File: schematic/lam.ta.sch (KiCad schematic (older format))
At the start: 14 parts, among them J1 Arduino_Nano_Header, P1 CONN_LED0, P10 CONN_TOUCH3, P2 CONN_LED1, P3 CONN_LED2, P4 CONN_LED3, P5 CONN_PSU, P6 CONN_LINE_IN, P7 CONN_TOUCH0, P8 CONN_TOUCH1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

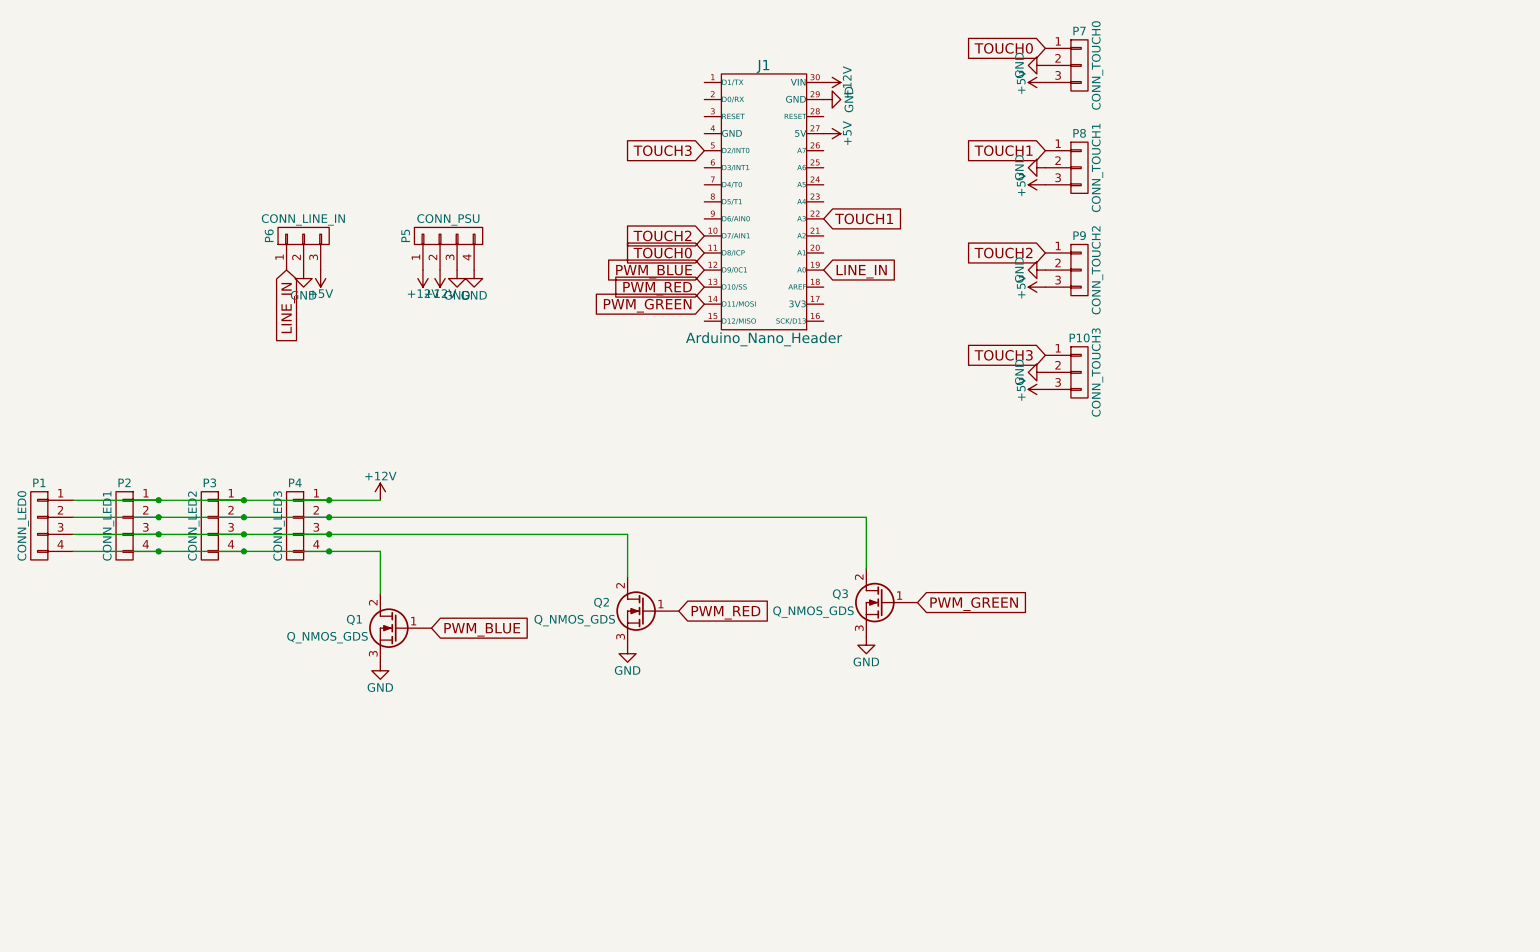
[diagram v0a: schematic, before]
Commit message: Update schematic license, replace AT42QT101X with MPR121
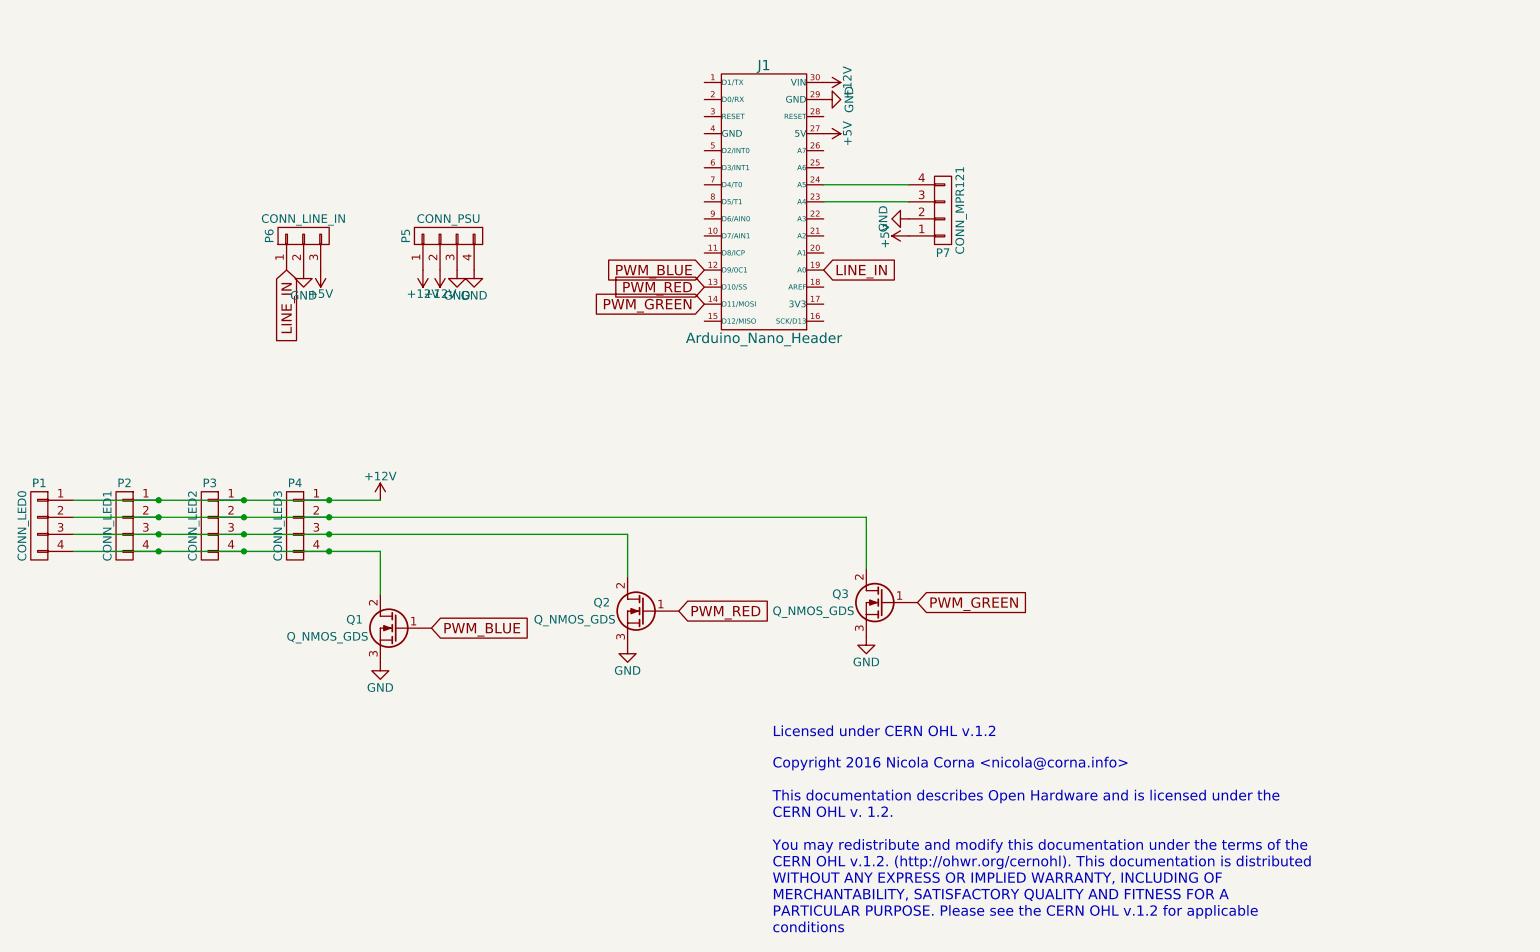
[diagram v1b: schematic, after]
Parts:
- removed P10: CONN_TOUCH3, Pin_Headers:Pin_Header_Straight_1x03, symbol CONN_01X03
- removed P7: CONN_TOUCH0, Pin_Headers:Pin_Header_Straight_1x03, symbol CONN_01X03
- removed P8: CONN_TOUCH1, Pin_Headers:Pin_Header_Straight_1x03, symbol CONN_01X03
- removed P9: CONN_TOUCH2, Pin_Headers:Pin_Header_Straight_1x03, symbol CONN_01X03
- added P7: CONN_MPR121, Pin_Headers:Pin_Header_Straight_1x04, symbol CONN_01X04
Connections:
- net +5V: now also P7.1 (P1)
- net GND: now also P7.2 (P2)
- net at J1.23 (A4): now also P7.3 (P3)
- net at J1.24 (A5): now also P7.4 (P4)
- net TOUCH0: no longer names the net of J1.11 (D8/ICP)
- net TOUCH1: no longer names the net of J1.22 (A3)
- net TOUCH2: no longer names the net of J1.10 (D7/AIN1)
- net TOUCH3: no longer names the net of J1.5 (D2/INT0)
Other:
- note added: "Copyright 2016 Nicola Corna <nicola@corna.info>\n\nThis documentation describes Open Hardware and is licensed under the\nCERN OHL v. 1.2.\n\nYou may redistribute and modify this documentation under the terms of the\nCERN OHL v.1.2. (http://ohwr.org/cernohl). This documentation is distributed\nWITHOUT ANY EXPRESS OR IMPLIED WARRANTY, INCLUDING OF\nMERCHANTABILITY, SATISFACTORY QUALITY AND FITNESS 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"
- note added: "Licensed under CERN OHL v.1.2"
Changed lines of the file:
@@
 encoding utf-8
 Sheet 1 1
-Title ""
-Date ""
-Rev ""
-Comp ""
-Comment1 ""
+Title "LAM.TA"
+Date "2016-03-14"
+Rev "1.0"
+Comp "Nicola Corna"
+Comment1 "Copyright 2016 Nicola Corna <nicola@corna.info>"
 Comment2 ""
 Comment3 ""
@@
 	1    0    0    -1
 $EndComp
-Text GLabel 6700 2350 0    60   Input ~ 0
-TOUCH0
-Text GLabel 7400 2150 2    60   Input ~ 0
-TOUCH1
-Text GLabel 6700 2250 0    60   Input ~ 0
-TOUCH2
-Text GLabel 6700 1750 0    60   Input ~ 0
-TOUCH3
-$Comp
-L CONN_01X03 P7
-U 1 1 56CADC43
-P 8900 1250
-F 0 "P7" H 8900 1450 50  0000 C CNN
-F 1 "CONN_TOUCH0" V 9000 1250 50  0000 C CNN
-F 2 "Pin_Headers:Pin_Header_Straight_1x03" H 8900 1250 50  0001 C CNN
-F 3 "" H 8900 1250 50  0000 C CNN
-	1    8900 1250
-	1    0    0    -1
-$EndComp
 $Comp
 L GND #PWR01
-U 1 1 56CADCB2
-P 8700 1250
-F 0 "#PWR01" H 8700 1000 50  0001 C CNN
-F 1 "GND" H 8700 1100 50  0000 C CNN
-F 2 "" H 8700 1250 50  0000 C CNN
-F 3 "" H 8700 1250 50  0000 C CNN
-	1    8700 1250
-	0    1    1    0
-$EndComp
-Text GLabel 8700 1150 0    60   Input ~ 0
-TOUCH0
-$Comp
-L CONN_01X03 P8
-U 1 1 56CADD7C
-P 8900 1850
-F 0 "P8" H 8900 2050 50  0000 C CNN
-F 1 "CONN_TOUCH1" V 9000 1850 50  0000 C CNN
-F 2 "Pin_Headers:Pin_Header_Straight_1x03" H 8900 1850 50  0001 C CNN
-F 3 "" H 8900 1850 50  0000 C CNN
-	1    8900 1850
-	1    0    0    -1
-$EndComp
-$Comp
-L GND #PWR02
-U 1 1 56CADD82
-P 8700 1850
-F 0 "#PWR02" H 8700 1600 50  0001 C CNN
-F 1 "GND" H 8700 1700 50  0000 C CNN
-F 2 "" H 8700 1850 50  0000 C CNN
-F 3 "" H 8700 1850 50  0000 C CNN
-	1    8700 1850
-	0    1    1    0
-$EndComp
-Text GLabel 8700 1750 0    60   Input ~ 0
-TOUCH1
-$Comp
-L CONN_01X03 P9
-U 1 1 56CADDB1
-P 8900 2450
-F 0 "P9" H 8900 2650 50  0000 C CNN
-F 1 "CONN_TOUCH2" V 9000 2450 50  0000 C CNN
-F 2 "Pin_Headers:Pin_Header_Straight_1x03" H 8900 2450 50  0001 C CNN
-F 3 "" H 8900 2450 50  0000 C CNN
-	1    8900 2450
-	1    0    0    -1
-$EndComp
-$Comp
-L GND #PWR03
-U 1 1 56CADDB7
-P 8700 2450
-F 0 "#PWR03" H 8700 2200 50  0001 C CNN
-F 1 "GND" H 8700 2300 50  0000 C CNN
-F 2 "" H 8700 2450 50  0000 C CNN
-F 3 "" H 8700 2450 50  0000 C CNN
-	1    8700 2450
-	0    1    1    0
-$EndComp
-Text GLabel 8700 2350 0    60   Input ~ 0
-TOUCH2
-$Comp
-L CONN_01X03 P10
-U 1 1 56CADDF4
-P 8900 3050
-F 0 "P10" H 8900 3250 50  0000 C CNN
-F 1 "CONN_TOUCH3" V 9000 3050 50  0000 C CNN
-F 2 "Pin_Headers:Pin_Header_Straight_1x03" H 8900 3050 50  0001 C CNN
-F 3 "" H 8900 3050 50  0000 C CNN
-	1    8900 3050
-	1    0    0    -1
-$EndComp
-$Comp
-L GND #PWR04
-U 1 1 56CADDFA
-P 8700 3050
-F 0 "#PWR04" H 8700 2800 50  0001 C CNN
-F 1 "GND" H 8700 2900 50  0000 C CNN
-F 2 "" H 8700 3050 50  0000 C CNN
-F 3 "" H 8700 3050 50  0000 C CNN
-	1    8700 3050
-	0    1    1    0
-$EndComp
-Text GLabel 8700 2950 0    60   Input ~ 0
-TOUCH3
-$Comp
-L +5V #PWR05
-U 1 1 56CADEBE
-P 8700 1350
-F 0 "#PWR05" H 8700 1200 50  0001 C CNN
-F 1 "+5V" H 8700 1490 50  0000 C CNN
-F 2 "" H 8700 1350 50  0000 C CNN
-F 3 "" H 8700 1350 50  0000 C CNN
-	1    8700 1350
-	0    -1   -1   0
-$EndComp
-$Comp
-L +5V #PWR06
-U 1 1 56CADED8
-P 8700 1950
-F 0 "#PWR06" H 8700 1800 50  0001 C CNN
-F 1 "+5V" H 8700 2090 50  0000 C CNN
-F 2 "" H 8700 1950 50  0000 C CNN
-F 3 "" H 8700 1950 50  0000 C CNN
-	1    8700 1950
-	0    -1   -1   0
-$EndComp
-$Comp
-L +5V #PWR07
-U 1 1 56CADEF2
-P 8700 2550
-F 0 "#PWR07" H 8700 2400 50  0001 C CNN
-F 1 "+5V" H 8700 2690 50  0000 C CNN
-F 2 "" H 8700 2550 50  0000 C CNN
-F 3 "" H 8700 2550 50  0000 C CNN
-	1    8700 2550
-	0    -1   -1   0
-$EndComp
-$Comp
-L +5V #PWR08
-U 1 1 56CADF0C
-P 8700 3150
-F 0 "#PWR08" H 8700 3000 50  0001 C CNN
-F 1 "+5V" H 8700 3290 50  0000 C CNN
-F 2 "" H 8700 3150 50  0000 C CNN
-F 3 "" H 8700 3150 50  0000 C CNN
-	1    8700 3150
-	0    -1   -1   0
-$EndComp
-$Comp
-L GND #PWR09
 U 1 1 56CAE7F3
 P 7400 1450
-F 0 "#PWR09" H 7400 1200 50  0001 C CNN
+F 0 "#PWR01" H 7400 1200 50  0001 C CNN
 F 1 "GND" H 7400 1300 50  0000 C CNN
 F 2 "" H 7400 1450 50  0000 C CNN
@@
 $EndComp
 $Comp
-L +12V #PWR010
+L +12V #PWR02
 U 1 1 56CB1BE7
 P 4800 3800
-F 0 "#PWR010" H 4800 3650 50  0001 C CNN
+F 0 "#PWR02" H 4800 3650 50  0001 C CNN
 F 1 "+12V" H 4800 3940 50  0000 C CNN
 F 2 "" H 4800 3800 50  0000 C CNN
@@
 $EndComp
 $Comp
-L +12V #PWR011
+L +12V #PWR03
 U 1 1 56CB2CF0
 P 5050 2450
-F 0 "#PWR011" H 5050 2300 50  0001 C CNN
+F 0 "#PWR03" H 5050 2300 50  0001 C CNN
 F 1 "+12V" H 5050 2590 50  0000 C CNN
 F 2 "" H 5050 2450 50  0000 C CNN
@@
 $EndComp
 $Comp
-L +12V #PWR012
+L +12V #PWR04
 U 1 1 56CC30C5
 P 5150 2450
-F 0 "#PWR012" H 5150 2300 50  0001 C CNN
+F 0 "#PWR04" H 5150 2300 50  0001 C CNN
 F 1 "+12V" H 5150 2590 50  0000 C CNN
 F 2 "" H 5150 2450 50  0000 C CNN
@@
 $EndComp
 $Comp
-L GND #PWR013
+L GND #PWR05
 U 1 1 56CF1E20
 P 5250 2450
-F 0 "#PWR013" H 5250 2200 50  0001 C CNN
+F 0 "#PWR05" H 5250 2200 50  0001 C CNN
 F 1 "GND" H 5250 2300 50  0000 C CNN
 F 2 "" H 5250 2450 50  0000 C CNN
@@
 $EndComp
 $Comp
-L GND #PWR014
+L GND #PWR06
 U 1 1 56CF1E4E
 P 5350 2450
-F 0 "#PWR014" H 5350 2200 50  0001 C CNN
+F 0 "#PWR06" H 5350 2200 50  0001 C CNN
 F 1 "GND" H 5350 2300 50  0000 C CNN
 F 2 "" H 5350 2450 50  0000 C CNN
@@
 $EndComp
 $Comp
-L GND #PWR015
+L GND #PWR07
 U 1 1 56CF1FCE
 P 4800 4750
-F 0 "#PWR015" H 4800 4500 50  0001 C CNN
+F 0 "#PWR07" H 4800 4500 50  0001 C CNN
 F 1 "GND" H 4800 4600 50  0000 C CNN
 F 2 "" H 4800 4750 50  0000 C CNN
@@
 $EndComp
 $Comp
-L GND #PWR016
+L GND #PWR08
 U 1 1 56CF1FFC
 P 6250 4650
-F 0 "#PWR016" H 6250 4400 50  0001 C CNN
+F 0 "#PWR08" H 6250 4400 50  0001 C CNN
 F 1 "GND" H 6250 4500 50  0000 C CNN
 F 2 "" H 6250 4650 50  0000 C CNN
@@
 $EndComp
 $Comp
-L GND #PWR017
+L GND #PWR09
 U 1 1 56CF205E
 P 7650 4600
-F 0 "#PWR017" H 7650 4350 50  0001 C CNN
+F 0 "#PWR09" H 7650 4350 50  0001 C CNN
 F 1 "GND" H 7650 4450 50  0000 C CNN
 F 2 "" H 7650 4600 50  0000 C CNN
@@
 $EndComp
 $Comp
-L +12V #PWR018
+L +12V #PWR010
 U 1 1 56CF2256
 P 7400 1350
-F 0 "#PWR018" H 7400 1200 50  0001 C CNN
+F 0 "#PWR010" H 7400 1200 50  0001 C CNN
 F 1 "+12V" H 7400 1490 50  0000 C CNN
 F 2 "" H 7400 1350 50  0000 C CNN
@@
 $EndComp
 $Comp
-L +5V #PWR019
+L +5V #PWR011
 U 1 1 56CF2284
 P 7400 1650
-F 0 "#PWR019" H 7400 1500 50  0001 C CNN
+F 0 "#PWR011" H 7400 1500 50  0001 C CNN
 F 1 "+5V" H 7400 1790 50  0000 C CNN
 F 2 "" H 7400 1650 50  0000 C CNN
@@
 $EndComp
 $Comp
-L GND #PWR020
+L GND #PWR012
 U 1 1 56CF286B
 P 4350 2450
-F 0 "#PWR020" H 4350 2200 50  0001 C CNN
+F 0 "#PWR012" H 4350 2200 50  0001 C CNN
 F 1 "GND" H 4350 2300 50  0000 C CNN
 F 2 "" H 4350 2450 50  0000 C CNN
@@
 $EndComp
 $Comp
-L +5V #PWR021
+L +5V #PWR013
 U 1 1 56CF2871
 P 4450 2450
-F 0 "#PWR021" H 4450 2300 50  0001 C CNN
+F 0 "#PWR013" H 4450 2300 50  0001 C CNN
 F 1 "+5V" H 4450 2590 50  0000 C CNN
 F 2 "" H 4450 2450 50  0000 C CNN
@@
 Text GLabel 4250 2450 3    60   Input ~ 0
 LINE_IN
+$Comp
+L CONN_01X04 P7
+U 1 1 56E6FEC6
+P 8100 2100
+F 0 "P7" H 8100 2350 50  0000 C CNN
+F 1 "CONN_MPR121" V 8200 2100 50  0000 C CNN
+F 2 "Pin_Headers:Pin_Header_Straight_1x04" H 8100 2100 50  0001 C CNN
+F 3 "" H 8100 2100 50  0000 C CNN
+	1    8100 2100
+	1    0    0    1
+$EndComp
+Wire Wire Line
+	7400 2050 7900 2050
+Wire Wire Line
+	7900 1950 7400 1950
+$Comp
+L +5V #PWR014
+U 1 1 56E7007B
+P 7900 2250
+F 0 "#PWR014" H 7900 2100 50  0001 C CNN
+F 1 "+5V" H 7900 2390 50  0000 C CNN
+F 2 "" H 7900 2250 50  0000 C CNN
+F 3 "" H 7900 2250 50  0000 C CNN
+	1    7900 2250
+	0    -1   -1   0
+$EndComp
+$Comp
+L GND #PWR015
+U 1 1 56E700AE
+P 7900 2150
+F 0 "#PWR015" H 7900 1900 50  0001 C CNN
+F 1 "GND" H 7900 2000 50  0000 C CNN
+F 2 "" H 7900 2150 50  0000 C CNN
+F 3 "" H 7900 2150 50  0000 C CNN
+	1    7900 2150
+	0    1    1    0
+$EndComp
+Text Notes 7100 5200 0    60   ~ 0
+Licensed under CERN OHL v.1.2
+Text Notes 7100 6350 0    60   ~ 0
+Copyright 2016 Nicola Corna <nicola@corna.info>\n\nThis documentation describes Open Hardware and is licensed under the\nCERN OHL v. 1.2.\n\nYou may redistribute and modify this documentation under the terms of the\nCERN OHL v.1.2. (http://ohwr.org/cernohl). This documentation is distributed\nWITHOUT ANY EXPRESS OR IMPLIED WARRANTY, INCLUDING OF\nMERCHANTABILITY, SATISFACTORY QUALITY AND FITNESS FOR A\nPARTICULAR PURPOSE. Please see the CERN OHL v.1.2 for applicable\nconditions
 $EndSCHEMATC
